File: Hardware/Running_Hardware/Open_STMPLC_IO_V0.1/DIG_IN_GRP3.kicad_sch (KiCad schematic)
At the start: 54 parts, among them J27 Screw_Terminal_01x02, J28 Screw_Terminal_01x02, J29 Screw_Terminal_01x02, J30 Screw_Terminal_01x02, J31 Screw_Terminal_01x02, J32 Screw_Terminal_01x02, U31 6N137, U32 6N137, U33 6N137, U34 6N137, U35 6N137, U36 6N137

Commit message: Analog input section
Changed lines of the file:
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@@
 			(effects
 				(font
-					(size 1.27 1.27)
+					(size 1 1)
 				)
 				(justify left)
@@
 			(effects
 				(font
-					(size 1.27 1.27)
+					(size 1 1)
 				)
 				(justify left)
@@
 			(effects
 				(font
-					(size 1.27 1.27)
+					(size 1 1)
 				)
 			)
@@
 			(effects
 				(font
-					(size 1.27 1.27)
+					(size 1 1)
 				)
 			)
@@
 			(effects
 				(font
-					(size 1.27 1.27)
+					(size 1 1)
 				)
 			)
@@
 			(effects
 				(font
-					(size 1.27 1.27)
+					(size 1 1)
 				)
 			)
@@
 			(effects
 				(font
-					(size 1.27 1.27)
+					(size 1 1)
 				)
 			)
@@
 			(effects
 				(font
-					(size 1.27 1.27)
+					(size 1 1)
 				)
 			)
@@
 			(effects
 				(font
-					(size 1.27 1.27)
+					(size 1 1)
 				)
 				(justify left)
@@
 			(effects
 				(font
-					(size 1.27 1.27)
+					(size 1 1)
 				)
 				(justify left)
@@
 			(effects
 				(font
-					(size 1.27 1.27)
+					(size 1 1)
 				)
 			)
@@
 			(effects
 				(font
-					(size 1.27 1.27)
+					(size 1 1)
 				)
 			)
@@
 			(effects
 				(font
-					(size 1.27 1.27)
+					(size 1 1)
 				)
 				(justify left)
@@
 			(effects
 				(font
-					(size 1.27 1.27)
+					(size 1 1)
 				)
 				(justify left)
@@
 			(effects
 				(font
-					(size 1.27 1.27)
+					(size 1 1)
 				)
 				(justify left)
@@
 			(effects
 				(font
-					(size 1.27 1.27)
+					(size 1 1)
 				)
 				(justify left)
@@
 			(effects
 				(font
-					(size 1.27 1.27)
+					(size 1 1)
 				)
 				(justify left)
@@
 			(effects
 				(font
-					(size 1.27 1.27)
+					(size 1 1)
 				)
 				(justify left)
@@
 			(effects
 				(font
-					(size 1.27 1.27)
+					(size 1 1)
 				)
 			)
@@
 			(effects
 				(font
-					(size 1.27 1.27)
+					(size 1 1)
 				)
 			)
@@
 			(effects
 				(font
-					(size 1.27 1.27)
+					(size 1 1)
 				)
 				(justify left)
@@
 			(effects
 				(font
-					(size 1.27 1.27)
+					(size 1 1)
 				)
 				(justify left)
@@
 			(effects
 				(font
-					(size 1.27 1.27)
+					(size 1 1)
 				)
 			)
@@
 			(effects
 				(font
-					(size 1.27 1.27)
+					(size 1 1)
 				)
 			)

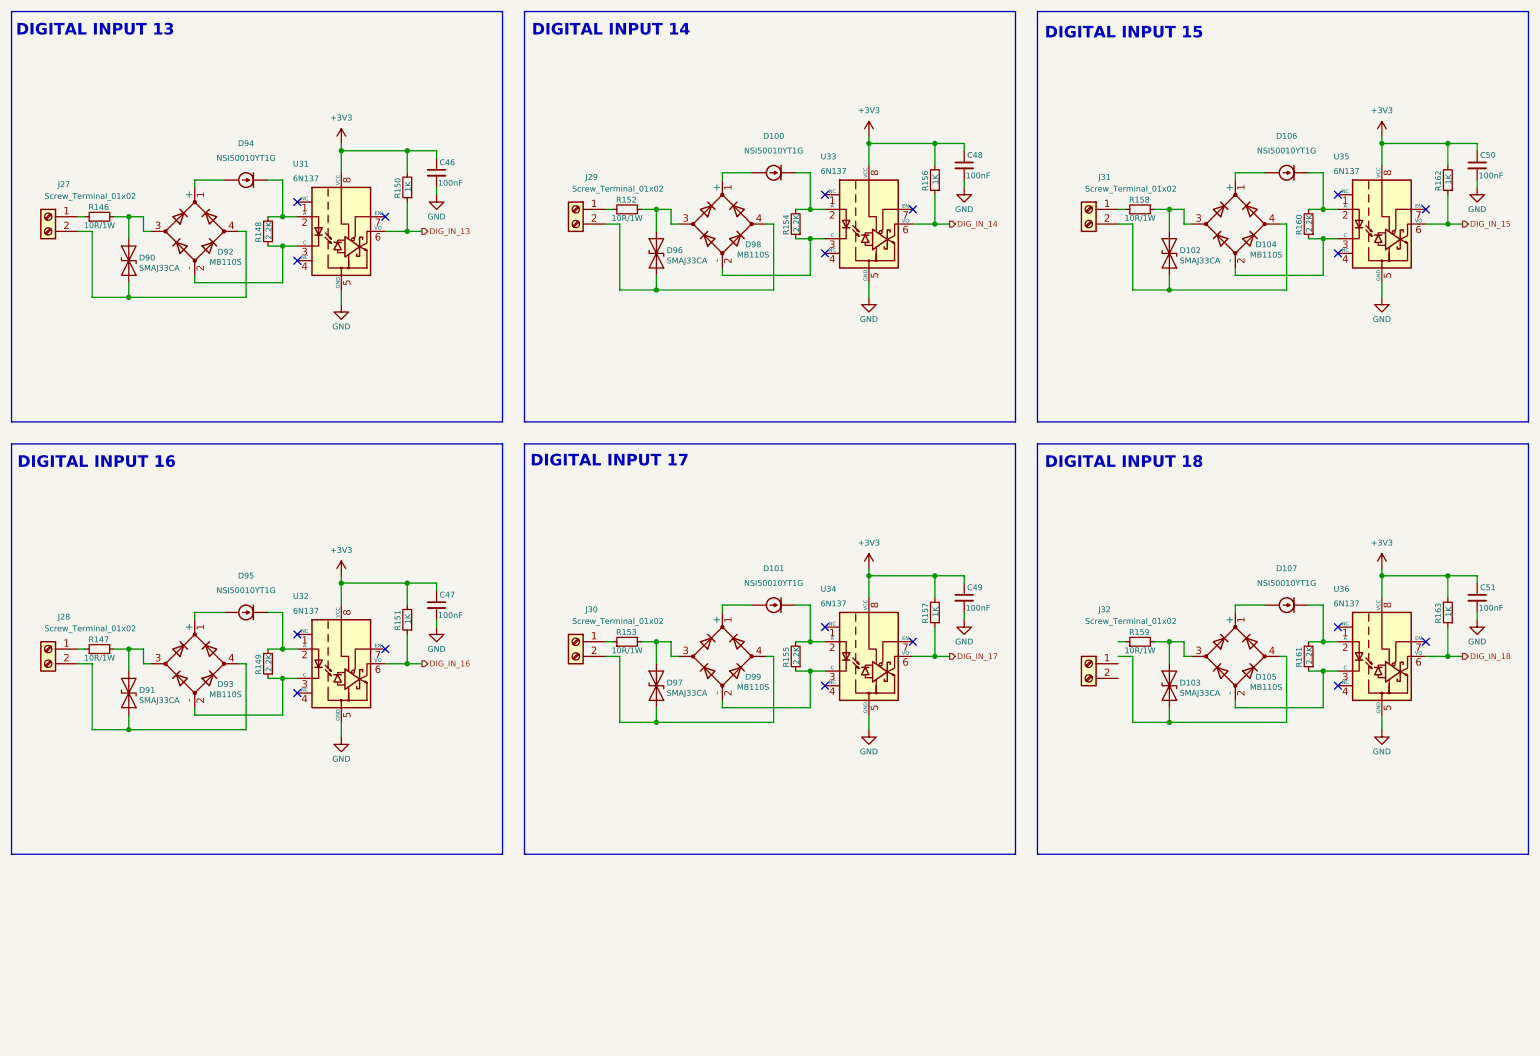
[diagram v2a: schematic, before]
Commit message: GSM Module add
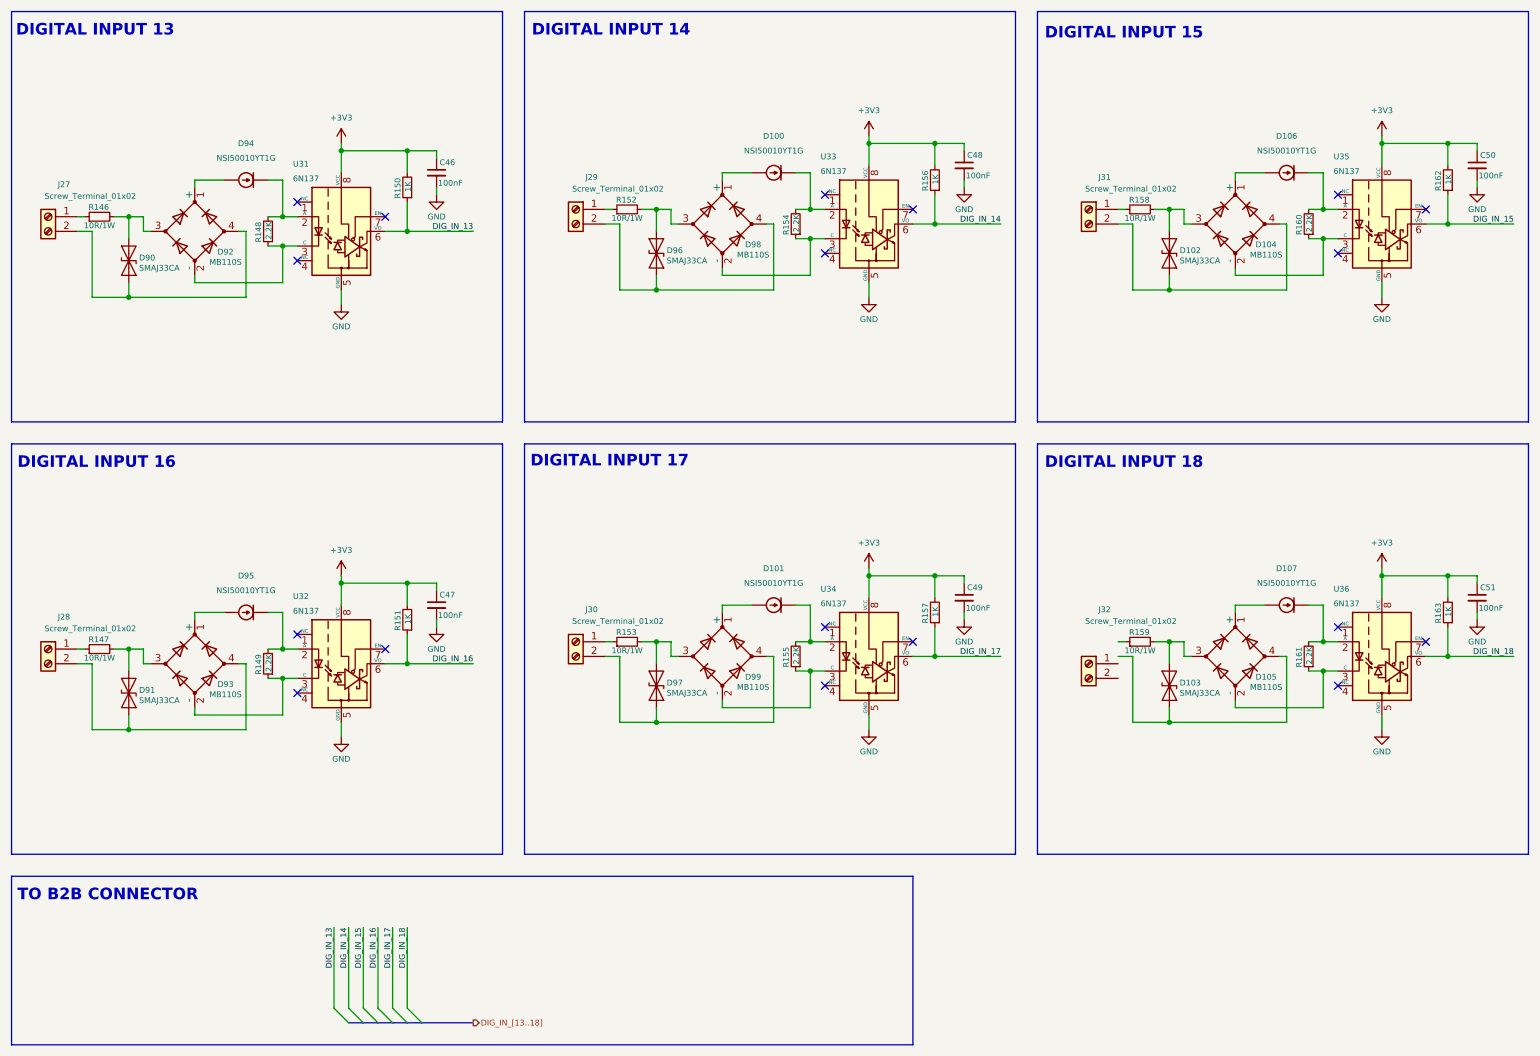
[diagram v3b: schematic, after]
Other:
- note added: "TO B2B CONNECTOR"
- title: (none) -> Open_PLC_IO

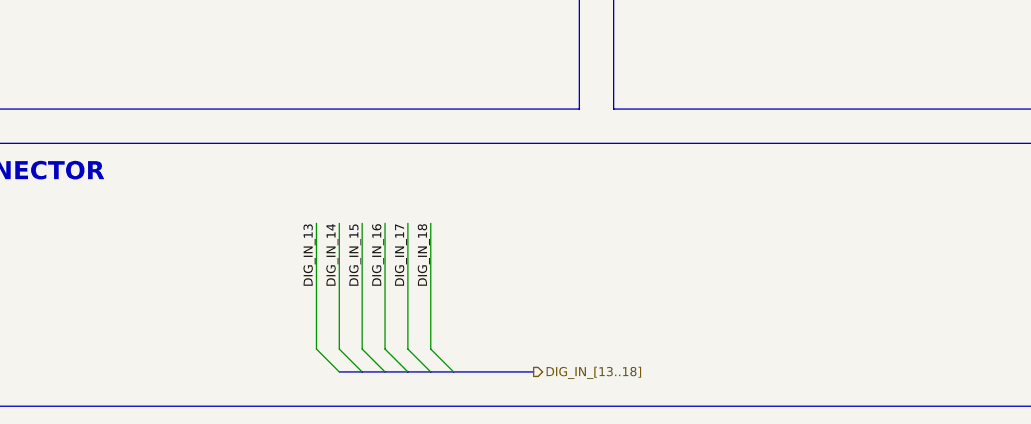
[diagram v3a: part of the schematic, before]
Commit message: Main PCB schematic changes V0.1
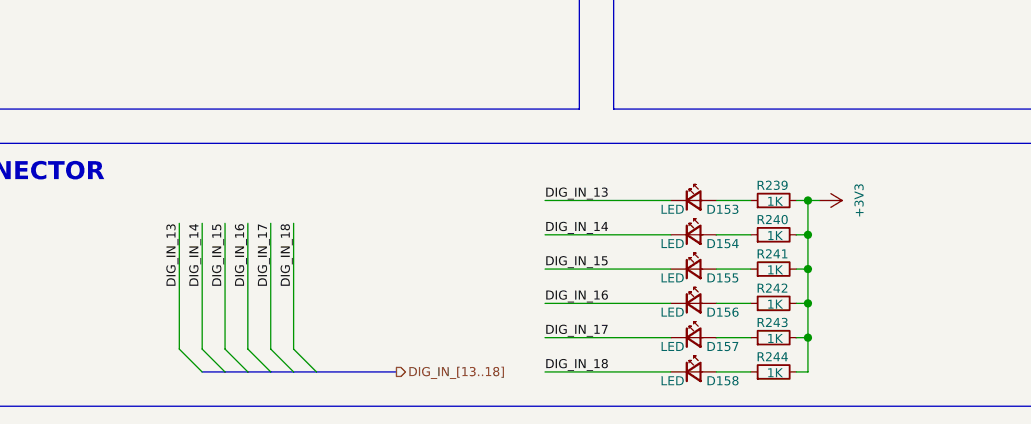
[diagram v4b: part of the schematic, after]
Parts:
- added D153, D154, D155, D156, D157, D158: LED, LED_SMD:LED_0603_1608Metric_Pad1.05x0.95mm_HandSolder, symbol Device:LED_Small
- added R239, R240, R241, R242, R243, R244: 1K, Resistor_SMD:R_0603_1608Metric_Pad0.98x0.95mm_HandSolder, symbol Device:R_Small
- C46, C47, C48, C49, C50, C51: footprint (none) -> Capacitor_SMD:C_0603_1608Metric_Pad1.08x0.95mm_HandSolder
- J27, J28, J29, J30, J31, J32: footprint (none) -> TerminalBlock_Phoenix:TerminalBlock_Phoenix_MKDS-1,5-2_1x02_P5.00mm_Horizontal
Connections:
- net +3V3: now also R239.2, R240.2, R241.2, R242.2, R243.2, R244.2
- net DIG_IN_13: now also D153.1 (K)
- net DIG_IN_14: now also D154.1 (K)
- net DIG_IN_15: now also D155.1 (K)
- net DIG_IN_16: now also D156.1 (K)
- net DIG_IN_17: now also D157.1 (K)
- net DIG_IN_18: now also D158.1 (K)
- new net: D158.2 (A), R244.1
- new net: D156.2 (A), R242.1
- new net: D154.2 (A), R240.1
- new net: D157.2 (A), R243.1
- new net: D153.2 (A), R239.1
- new net: D155.2 (A), R241.1
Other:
- title: Open_PLC_IO -> Open_STMPLC_IO

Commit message: New DXF update
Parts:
- J27, J28, J29, J30, J31, J32: footprint TerminalBlock_Phoenix:TerminalBlock_Phoenix_MKDS-1,5-2_1x02_P5.00mm_Horizontal -> TerminalBlock_Phoenix:TerminalBlock_Phoenix_MKDS-1-2-3.81_1x02_P3.81mm_Horizontal
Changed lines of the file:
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@@
 			)
 		)
-		(property "Footprint" "TerminalBlock_Phoenix:TerminalBlock_Phoenix_MKDS-1,5-2_1x02_P5.00mm_Horizontal"
+		(property "Footprint" "TerminalBlock_Phoenix:TerminalBlock_Phoenix_MKDS-1-2-3.81_1x02_P3.81mm_Horizontal"
 			(at 203.2 128.27 0)
 			(effects
@@
 			)
 		)
-		(property "Footprint" "TerminalBlock_Phoenix:TerminalBlock_Phoenix_MKDS-1,5-2_1x02_P5.00mm_Horizontal"
+		(property "Footprint" "TerminalBlock_Phoenix:TerminalBlock_Phoenix_MKDS-1-2-3.81_1x02_P3.81mm_Horizontal"
 			(at 114.3 124.46 0)
 			(effects
@@
 			)
 		)
-		(property "Footprint" "TerminalBlock_Phoenix:TerminalBlock_Phoenix_MKDS-1,5-2_1x02_P5.00mm_Horizontal"
+		(property "Footprint" "TerminalBlock_Phoenix:TerminalBlock_Phoenix_MKDS-1-2-3.81_1x02_P3.81mm_Horizontal"
 			(at 22.86 50.8 0)
 			(effects
@@
 			)
 		)
-		(property "Footprint" "TerminalBlock_Phoenix:TerminalBlock_Phoenix_MKDS-1,5-2_1x02_P5.00mm_Horizontal"
+		(property "Footprint" "TerminalBlock_Phoenix:TerminalBlock_Phoenix_MKDS-1-2-3.81_1x02_P3.81mm_Horizontal"
 			(at 114.3 49.53 0)
 			(effects
@@
 			)
 		)
-		(property "Footprint" "TerminalBlock_Phoenix:TerminalBlock_Phoenix_MKDS-1,5-2_1x02_P5.00mm_Horizontal"
+		(property "Footprint" "TerminalBlock_Phoenix:TerminalBlock_Phoenix_MKDS-1-2-3.81_1x02_P3.81mm_Horizontal"
 			(at 203.2 49.53 0)
 			(effects
@@
 			)
 		)
-		(property "Footprint" "TerminalBlock_Phoenix:TerminalBlock_Phoenix_MKDS-1,5-2_1x02_P5.00mm_Horizontal"
+		(property "Footprint" "TerminalBlock_Phoenix:TerminalBlock_Phoenix_MKDS-1-2-3.81_1x02_P3.81mm_Horizontal"
 			(at 22.86 125.73 0)
 			(effects
